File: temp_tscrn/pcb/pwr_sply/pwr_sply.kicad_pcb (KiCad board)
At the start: 2 copper layers, 55 x 38 mm, 9 parts, among them J1 Screw_Terminal_01x03, J2 Conn_01x03_Male, Q1 Q_PMOS_GSD

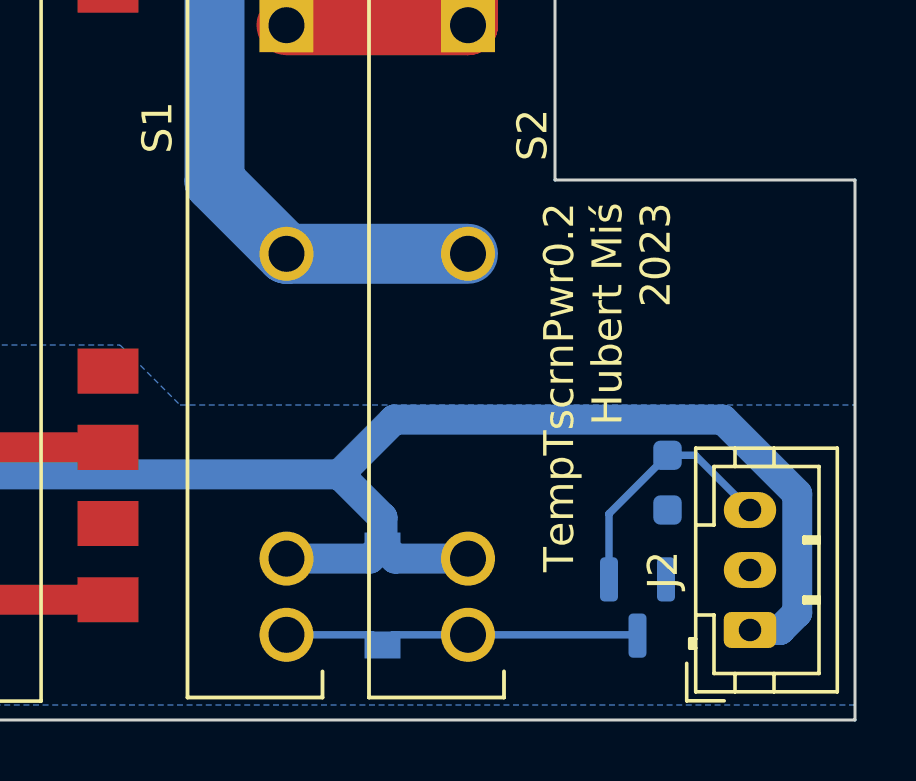
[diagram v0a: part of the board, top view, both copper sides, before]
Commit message: temp_tscrn: pcb: add ldo
Add LDO in the power supply board for compatibility with the display
board. Max current for LDO is 450 mA. The MOSFET should be fine if
controlled with 3.3V switching 5V for SSR control.
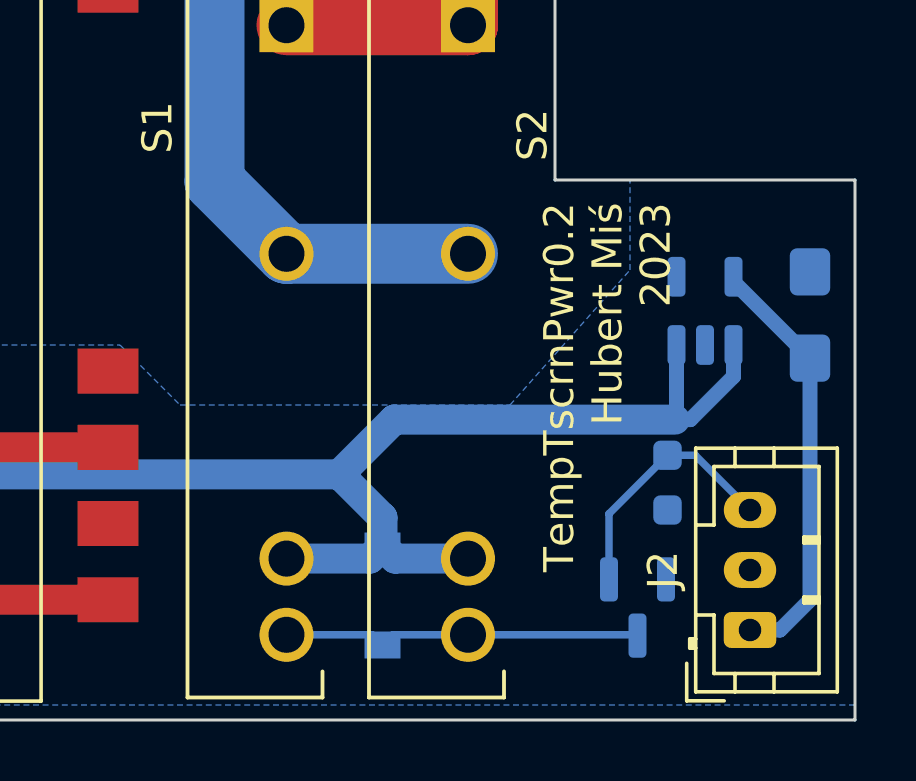
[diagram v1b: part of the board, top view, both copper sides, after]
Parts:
- added C2: C_Polarized, Capacitor_Tantalum_SMD:CP_EIA-3216-18_Kemet-A_Pad1.58x1.35mm_HandSolder, B.Cu at (103.5, 94.5)
- added U1: TLV75533PDBV, Package_TO_SOT_SMD:SOT-23-5, B.Cu at (100.0, 94.4)
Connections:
- J2 pad 1: VCC -> +3.3V
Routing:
- net +3.3V: track 0.00 -> 14.2 mm
- net VCC: track 54.0 -> 49.2 mm
